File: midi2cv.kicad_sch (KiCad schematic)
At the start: 23 parts, among them J1 AudioJack3, J2 Conn_02x05_Top_Bottom, J3 AudioJack2_SwitchT, J4 AudioJack2_SwitchT, J5 AudioJack2_SwitchT, J6 AudioJack2_SwitchT, J7 AudioJack3, Q1 BC548, U1 6N138

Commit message: routed pcb
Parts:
- removed C1: 100n, Capacitor_THT:C_Disc_D3.0mm_W2.0mm_P2.50mm, symbol Device:C
- removed C2, C3: 100p, Capacitor_THT:C_Disc_D3.0mm_W2.0mm_P2.50mm, symbol Device:C
- removed C4, C5, C6: 10u, Capacitor_THT:CP_Radial_D5.0mm_P2.00mm, symbol Device:C_Polarized
- removed D1: 1N4148, Diode_THT:D_DO-35_SOD27_P2.54mm_Vertical_AnodeUp, symbol Diode:1N4148
- removed J1, J7: AudioJack3, TRS_AudioConn3:Jack_3.5mm_QingPu_WQP-PJ366ST_Vertical, symbol Connector_Audio:AudioJack3
- removed J2: Conn_02x05_Top_Bottom, Connector_IDC:IDC-Header_2x05_P2.54mm_Vertical, symbol Connector_Generic:Conn_02x05_Odd_Even
- removed J3: AudioJack2_SwitchT, Connector_Audio:Jack_3.5mm_QingPu_WQP-PJ398SM_Vertical_CircularHoles, symbol Connector_Audio:AudioJack2_SwitchT
- removed Q1: BC548, Package_TO_SOT_THT:TO-92_Inline_Wide, symbol Transistor_BJT:BC548
- removed R1, R5, R6: 220R, Resistor_THT:R_Axial_DIN0207_L6.3mm_D2.5mm_P2.54mm_Vertical, symbol Device:R
- removed R2, R3, R4: 1k, Resistor_THT:R_Axial_DIN0207_L6.3mm_D2.5mm_P2.54mm_Vertical, symbol Device:R
- removed U1: 6N138, Package_DIP:DIP-8_W7.62mm_Socket_LongPads, symbol Isolator:6N138
- added B2: Board, Custom:Board_4hp_100mm, symbol Custom:Board
- added B3: Front_Plate, Custom:Front_Plate_4hp_cut, symbol Custom:Front_Plate
- added C17: 10n, Capacitor_SMD:C_0603_1608Metric, symbol Device:C
- added D5, D6: LED, LED_THT:LED_D3.0mm, symbol Device:LED
- added H1, H2, H3, H4, H5, H6, H7: 6mm, Custom:DrillHole_D6.00, symbol Custom:Mounting_Hole
- added H10: 7mm, Custom:DrillHole_D7.00, symbol Custom:Mounting_Hole
- added H8, H9: 3mm, Custom:DrillHole_D3.00, symbol Custom:Mounting_Hole
- added J9: Conn_02x04_Odd_Even, Connector_PinSocket_1.27mm:PinSocket_2x04_P1.27mm_Vertical, symbol Connector_Generic:Conn_02x04_Odd_Even
- added R11, R8, R9: 1k, Resistor_SMD:R_0603_1608Metric, symbol Device:R
- added R18: 100, Resistor_SMD:R_0603_1608Metric, symbol Device:R
- added R24, R27: 4k7, Resistor_SMD:R_0603_1608Metric, symbol Device:R
- added RV5: A100k, EuroRackTools:Potentiometer_Alpha_RD901F-40-00D_Single_Vertical, symbol Device:R_Potentiometer
- J4: value AudioJack2_SwitchT -> Clock; footprint Connector_Audio:Jack_3.5mm_QingPu_WQP-PJ398SM_Vertical_CircularHoles -> Custom:Jack_3.5mm_QingPu_WQP-PJ398SM_Vertical_CircularHoles_L
- J5: value AudioJack2_SwitchT -> Clock2; footprint Connector_Audio:Jack_3.5mm_QingPu_WQP-PJ398SM_Vertical_CircularHoles -> Custom:Jack_3.5mm_QingPu_WQP-PJ398SM_Vertical_CircularHoles_L
- J6: value AudioJack2_SwitchT -> Gate; footprint Connector_Audio:Jack_3.5mm_QingPu_WQP-PJ398SM_Vertical_CircularHoles -> Custom:Jack_3.5mm_QingPu_WQP-PJ398SM_Vertical_CircularHoles_L
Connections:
- net B_+12V: now also J9.2 (Pin_2)
- net B_+5V: now also J9.8 (Pin_8)
- net B_-12V: now also J9.6 (Pin_6)
- net B_GND: now also A1.29 (GND), C17.2, J9.4 (Pin_4)
- net C_GND: now also J4.S, J5.S, J6.S, R24.2, R27.2
- net MIDI_IN: now also A1.21 (A2)
- net CLOCK: now reaches A1.1 (D1/TX)
- net CLOCK: now also R8.2
- net EXP5: now reaches A1.14 (D11)
- net EXP5: now also J9.5 (Pin_5)
- net CLOCK2: now reaches A1.2 (D0/RX)
- net CLOCK2: now also D5.2 (A), R9.2
- net GATE: now reaches A1.26 (A7)
- net GATE: now also D6.2 (A), R11.2
- net EXP1: now reaches A1.6 (D3)
- net EXP1: now also J9.1 (Pin_1)
- net EXP3: now reaches A1.8 (D5)
- net EXP3: now also J9.3 (Pin_3)
- net EXP7: now reaches A1.9 (D6)
- net EXP7: now also J9.7 (Pin_7)
- net at J5.T: now also R9.1
- net at J6.T: now also R11.1
- net at J4.T: now also R8.1
- net PWM_H renamed CC
- net PWM_L renamed PITCH
- new net: D6.1 (K), R27.1
- new net: R18.1, RV5.1
- new net: D5.1 (K), R24.1
- new net SLEW_IN: R18.2
- new net SLEW_OUT: C17.1, RV5.2, RV5.3
- no-connect marks 0 -> 19
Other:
- added sheet MIDI_IO (MIDI_IO.kicad_sch)
- added sheet PitchOutput (PitchOutput.kicad_sch)
- added sheet Power (Power.kicad_sch)
- note added: "24ppqn (MIDI / DIN Sync)"
- note added: "4ppqn (16th notes)"
- note added: "IDC Header for Gate Expansion Module"
- note added: "Slew"
- note removed: "2N5551 could be an other choice"
- note removed: "CV Out"
- note removed: "MIDI IN"
- note removed: "MIDI Through"
- note removed: "Reset Out"
- note removed: "TODO: 2 Pin PWM"
- note removed: "TODO: Transistor buffer"
- moved on the sheet: A1, J4, J5

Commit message: add gerbers and bom
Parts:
- A1, B2, B3, D5, D6, H1, H10, H2, H3, H4, H5, H6, H7, H8, H9, J4, J5, J6, J9, RV5: JLCPCB_IGNORE (none) -> 1
- C17: LCSC (none) -> C1589
- R11, R8, R9: LCSC (none) -> C21190
- R18: LCSC (none) -> C22775
- R24, R27: LCSC (none) -> C23162
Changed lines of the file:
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@@
 			)
 		)
-		(property "LCSC PN" ""
+		(property "LCSC" "C23162"
+			(at 165.1 120.65 0)
+			(effects
+				(font
+					(size 1.27 1.27)
+				)
+				(hide yes)
+			)
+		)
+		(property "JLCPCB_IGNORE" ""
 			(at 165.1 120.65 0)
 			(effects
@@
 			)
 		)
-		(property "LCSC PN" ""
+		(property "JLCPCB_IGNORE" "1"
 			(at 58.42 104.14 0)
 			(effects
@@
 			)
 		)
+		(property "JLCPCB_IGNORE" "1"
+			(at 260.35 48.26 0)
+			(effects
+				(font
+					(size 1.27 1.27)
+				)
+				(hide yes)
+			)
+		)
 		(instances
 			(project "midi2cv"
@@
 			)
 		)
+		(property "JLCPCB_IGNORE" "1"
+			(at 237.49 34.29 0)
+			(effects
+				(font
+					(size 1.27 1.27)
+				)
+				(hide yes)
+			)
+		)
 		(instances
 			(project ""
@@
 			)
 		)
-		(property "LCSC PN" ""
+		(property "LCSC" "C1589"
+			(at 73.66 50.8 0)
+			(effects
+				(font
+					(size 1.27 1.27)
+				)
+				(hide yes)
+			)
+		)
+		(property "JLCPCB_IGNORE" ""
 			(at 73.66 50.8 0)
 			(effects
@@
 			)
 		)
+		(property "JLCPCB_IGNORE" "1"
+			(at 231.14 101.6 0)
+			(effects
+				(font
+					(size 1.27 1.27)
+				)
+				(hide yes)
+			)
+		)
 		(pin "8"
 		)
@@
 			)
 		)
+		(property "JLCPCB_IGNORE" "1"
+			(at 256.54 55.88 0)
+			(effects
+				(font
+					(size 1.27 1.27)
+				)
+				(hide yes)
+			)
+		)
 		(instances
 			(project "midi2cv"
@@
 			)
 		)
+		(property "JLCPCB_IGNORE" "1"
+			(at 260.35 43.18 0)
+			(effects
+				(font
+					(size 1.27 1.27)
+				)
+				(hide yes)
+			)
+		)
 		(instances
 			(project ""
@@
 			)
 		)
-		(property "LCSC PN" ""
+		(property "LCSC" "C21190"
+			(at 171.45 101.6 90)
+			(effects
+				(font
+					(size 1.27 1.27)
+				)
+				(hide yes)
+			)
+		)
+		(property "JLCPCB_IGNORE" ""
 			(at 171.45 101.6 90)
 			(effects
@@
 			)
 		)
-		(property "LCSC PN" ""
+		(property "LCSC" "C21190"
+			(at 171.45 67.31 90)
+			(effects
+				(font
+					(size 1.27 1.27)
+				)
+				(hide yes)
+			)
+		)
+		(property "JLCPCB_IGNORE" ""
 			(at 171.45 67.31 90)
 			(effects
@@
 			)
 		)
+		(property "JLCPCB_IGNORE" "1"
+			(at 262.89 36.83 0)
+			(effects
+				(font
+					(size 1.27 1.27)
+				)
+				(hide yes)
+			)
+		)
 		(instances
 			(project "midi2cv"
@@
 			)
 		)
-		(property "LCSC PN" ""
+		(property "JLCPCB_IGNORE" "1"
 			(at 67.31 44.45 90)
 			(effects
@@
 			)
 		)
+		(property "JLCPCB_IGNORE" "1"
+			(at 262.89 62.23 0)
+			(effects
+				(font
+					(size 1.27 1.27)
+				)
+				(hide yes)
+			)
+		)
 		(instances
 			(project "midi2cv"
@@
 			)
 		)
+		(property "JLCPCB_IGNORE" "1"
+			(at 262.89 55.88 0)
+			(effects
+				(font
+					(size 1.27 1.27)
+				)
+				(hide yes)
+			)
+		)
 		(instances
 			(project "midi2cv"
@@
 			)
 		)
+		(property "JLCPCB_IGNORE" "1"
+			(at 256.54 31.75 0)
+			(effects
+				(font
+					(size 1.27 1.27)
+				)
+				(hide yes)
+			)
+		)
 		(instances
 			(project "midi2cv"
@@
 			)
 		)
-		(property "LCSC PN" ""
+		(property "LCSC" "C21190"
+			(at 171.45 38.1 90)
+			(effects
+				(font
+					(size 1.27 1.27)
+				)
+				(hide yes)
+			)
+		)
+		(property "JLCPCB_IGNORE" ""
 			(at 171.45 38.1 90)
 			(effects
@@
 			)
 		)
+		(property "JLCPCB_IGNORE" "1"
+			(at 262.89 31.75 0)
+			(effects
+				(font
+					(size 1.27 1.27)
+				)
+				(hide yes)
+			)
+		)
 		(instances
 			(project "midi2cv"
@@
 			)
 		)
+		(property "JLCPCB_IGNORE" "1"
+			(at 262.89 25.4 0)
+			(effects
+				(font
+					(size 1.27 1.27)
+				)
+				(hide yes)
+			)
+		)
 		(instances
 			(project "midi2cv"
@@
 			)
 		)
-		(property "LCSC PN" ""
+		(property "JLCPCB_IGNORE" "1"
 			(at 163.83 72.39 90)
 			(effects
@@
 			)
 		)
-		(property "LCSC PN" ""
+		(property "JLCPCB_IGNORE" "1"
 			(at 182.88 67.31 0)
 			(effects
@@
 			)
 		)
-		(property "LCSC PN" ""
+		(property "LCSC" "C22775"
+			(at 55.88 44.45 90)
+			(effects
+				(font
+					(size 1.27 1.27)
+				)
+				(hide yes)
+			)
+		)
+		(property "JLCPCB_IGNORE" ""
 			(at 55.88 44.45 90)
 			(effects
@@
 			)
 		)
-		(property "LCSC PN" ""
+		(property "LCSC" "C23162"
+			(at 163.83 81.28 0)
+			(effects
+				(font
+					(size 1.27 1.27)
+				)
+				(hide yes)
+			)
+		)
+		(property "JLCPCB_IGNORE" ""
 			(at 163.83 81.28 0)
 			(effects
@@
 			)
 		)
+		(property "JLCPCB_IGNORE" "1"
+			(at 256.54 25.4 0)
+			(effects
+				(font
+					(size 1.27 1.27)
+				)
+				(hide yes)
+			)
+		)
 		(instances
 			(project ""
@@
 			)
 		)
-		(property "LCSC PN" ""
+		(property "JLCPCB_IGNORE" "1"
 			(at 182.88 101.6 0)
 			(effects
@@
 			)
 		)
-		(property "LCSC PN" ""
+		(property "JLCPCB_IGNORE" "1"
 			(at 165.1 110.49 90)
 			(effects
@@
 			)
 		)
-		(property "LCSC PN" ""
+		(property "JLCPCB_IGNORE" "1"
 			(at 182.88 38.1 0)
 			(effects
@@
 			(at 256.54 62.23 0)
 			(effects
+				(font
+					(size 1.27 1.27)
+				)
+				(hide yes)
+			)
+		)
+		(property "JLCPCB_IGNORE" "1"
+			(at 256.54 62.23 0)
+			(effects

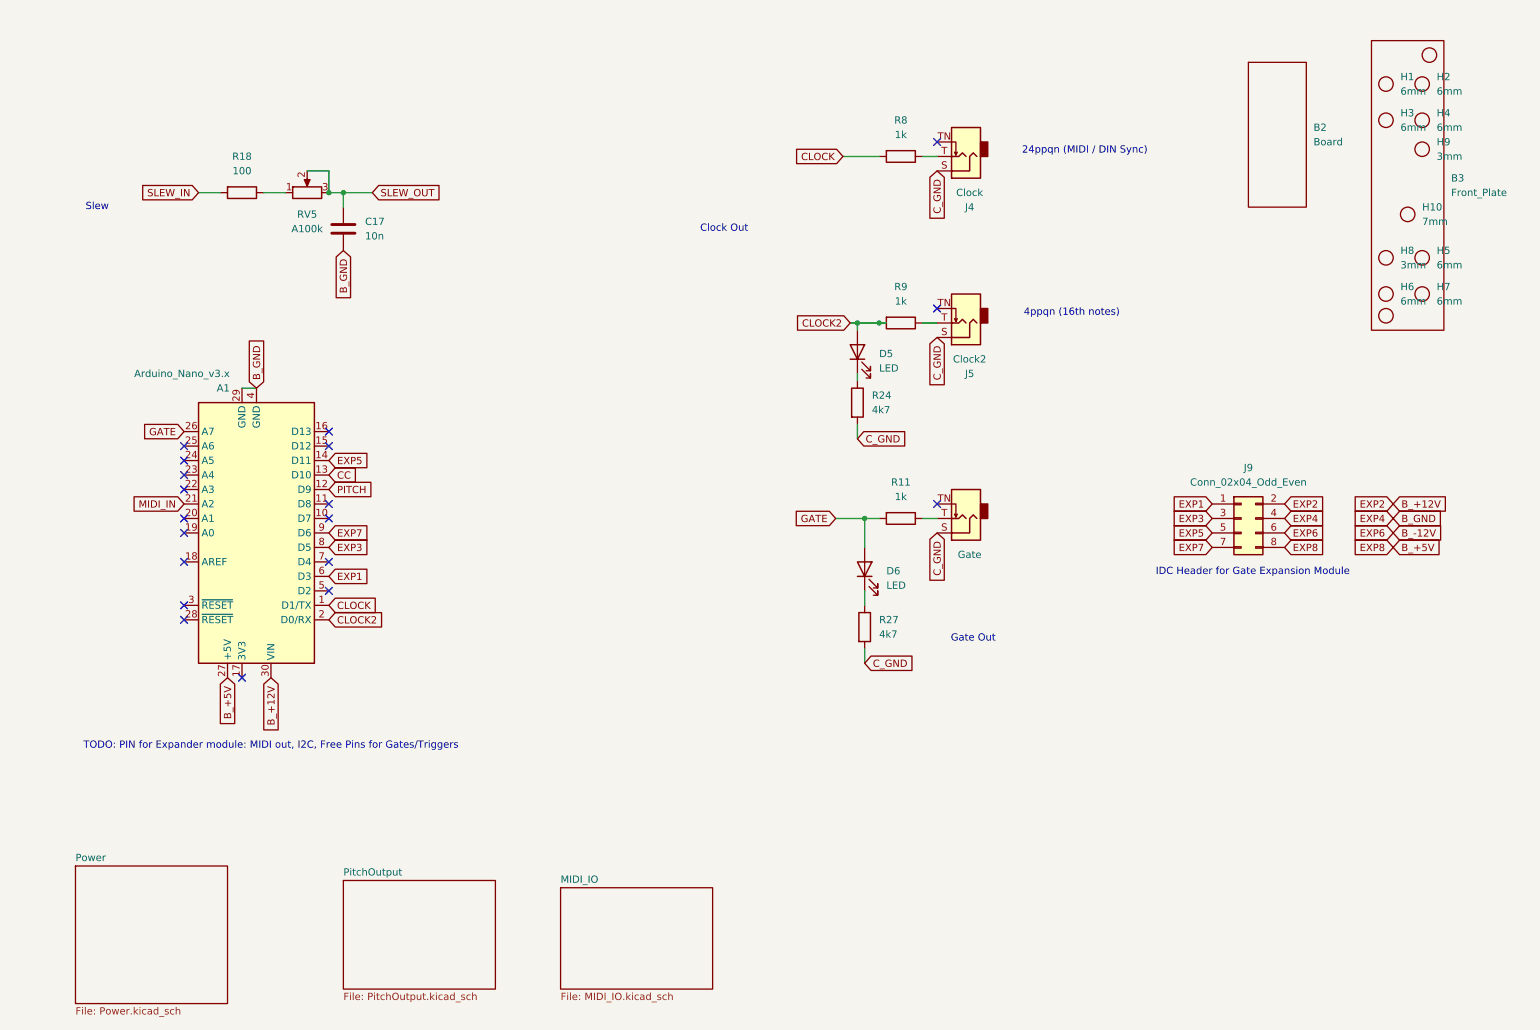
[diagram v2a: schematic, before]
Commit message: add rev 2 and rev 3, now with correct trs midi A
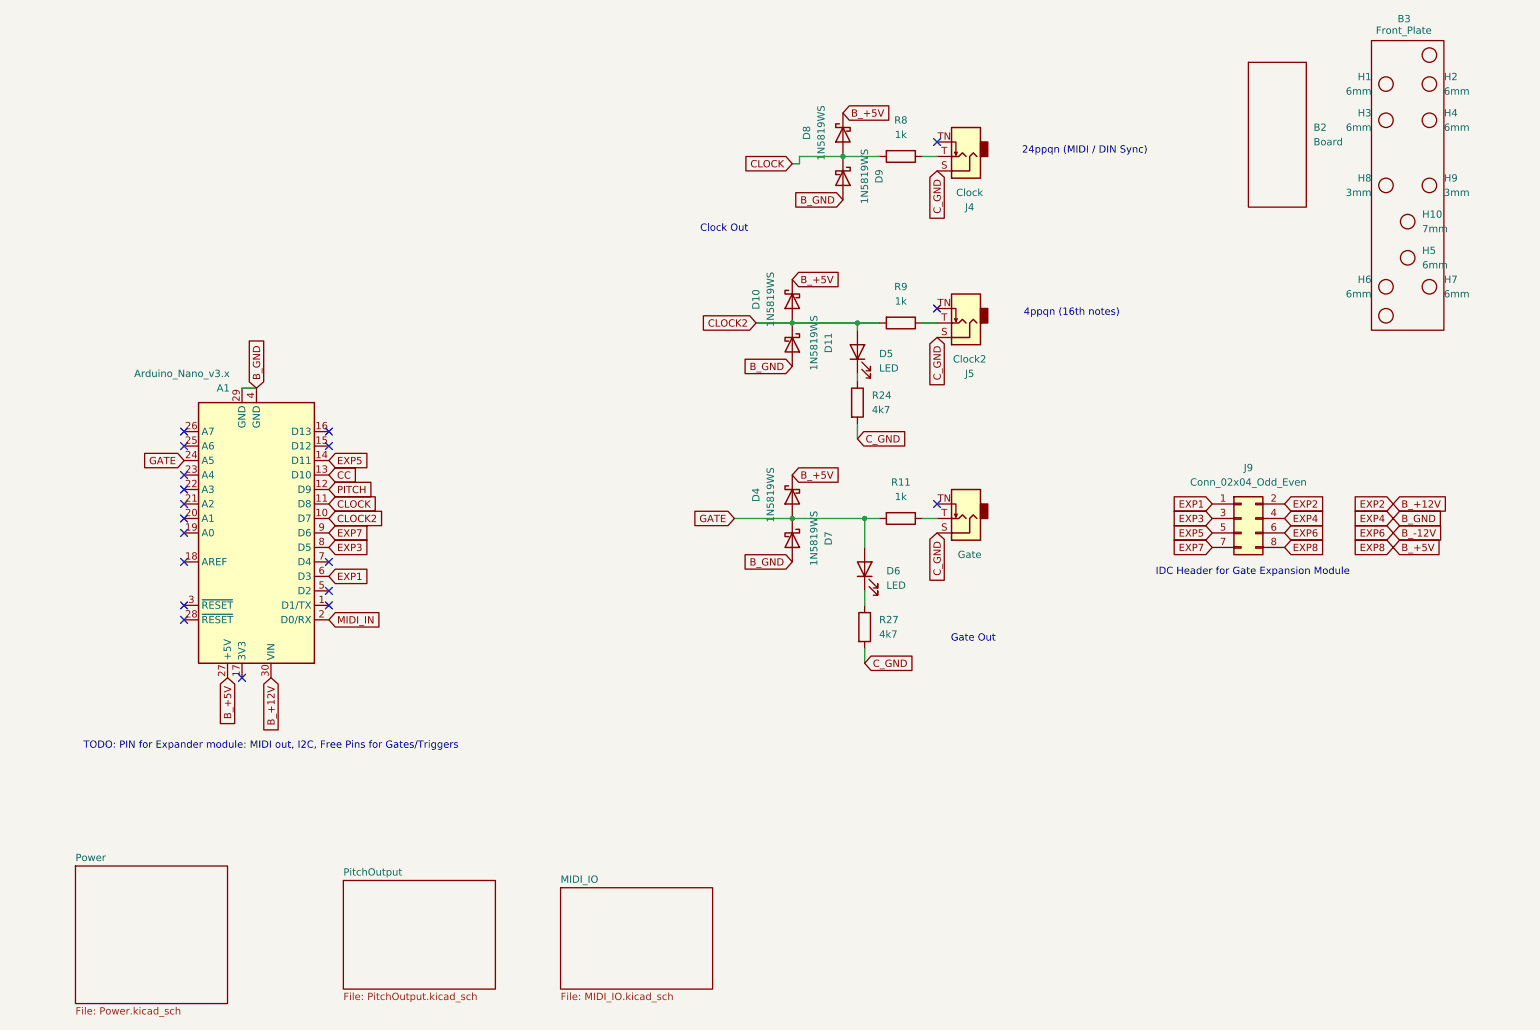
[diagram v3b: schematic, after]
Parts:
- removed C17: 10n, Capacitor_SMD:C_0603_1608Metric, symbol Device:C
- removed R18: 100, Resistor_SMD:R_0603_1608Metric, symbol Device:R
- removed RV5: A100k, EuroRackTools:Potentiometer_Alpha_RD901F-40-00D_Single_Vertical, symbol Device:R_Potentiometer
- added D10, D11, D4, D7, D8, D9: 1N5819WS, Diode_SMD:D_SOD-323, symbol Diode:1N5819WS
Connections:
- net B_+5V: now also D10.1 (K), D4.1 (K), D8.1 (K)
- net B_GND: now also D11.2 (A), D7.2 (A), D9.2 (A)
- net CLOCK: now also A1.11 (D8), D8.2 (A), D9.1 (K); no longer A1.1 (D1/TX)
- net CLOCK2: now also A1.10 (D7), D10.2 (A), D11.1 (K); no longer A1.2 (D0/RX)
- net GATE: now also A1.24 (A5), D4.2 (A), D7.1 (K); no longer A1.26 (A7)
- net MIDI_IN: now also A1.2 (D0/RX); no longer A1.21 (A2)
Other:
- note removed: "Slew"
- moved on the sheet: H10, H2, H4, H5, H6, H7, H8, H9
